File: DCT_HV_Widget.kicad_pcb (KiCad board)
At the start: 2 copper layers, 53.9 x 74.6 mm, 27 parts, among them J1 Control Voltage, J2 Bench Power Supply, J3 High Voltage, Q1 ZXTN10150D, U1 LT1468CS8-PBF, U2 OC150G

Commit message: Updated PCB. Rearranged bottom silkscreen layer.
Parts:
- moved G*** 9.75 mm to (160.9, 100.1)
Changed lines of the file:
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@@
       (drillshape 0)
       (scaleselection 1)
-      (outputdirectory "FLoBBr_Gerbers")
+      (outputdirectory "FLoBBr_Drill")
     )
   )
@@
   )
   (footprint "LOGO" (layer "B.Cu")
-    (at 163.615556 109.435583 180)
+    (at 160.875 100.075 180)
     (attr board_only exclude_from_pos_files exclude_from_bom)
     (fp_text reference "G***" (at 0 0) (layer "B.SilkS") hide
@@
   (gr_line (start 166.116 72.644) (end 175.768 72.644) (layer "F.SilkS") (width 0.15))
   (gr_rect (start 133.425 69.4) (end 187.375 144) (layer "Edge.Cuts") (width 0.1016) (fill none))
-  (gr_text "Fantastic Load Bearing Board\n(FLoBBr)" (at 159.766 83.058) (layer "B.SilkS")
-    (effects (font (size 2 2) (thickness 0.4)) (justify mirror))
+  (gr_text "Fantastic Load Bearing Board\n(FLoBBr)" (at 183.875 112.7 90) (layer "B.SilkS")
+    (effects (font (size 1.75 1.75) (thickness 0.3)) (justify mirror))
   )
   (gr_text "+" (at 146.925 89.15) (layer "F.SilkS")

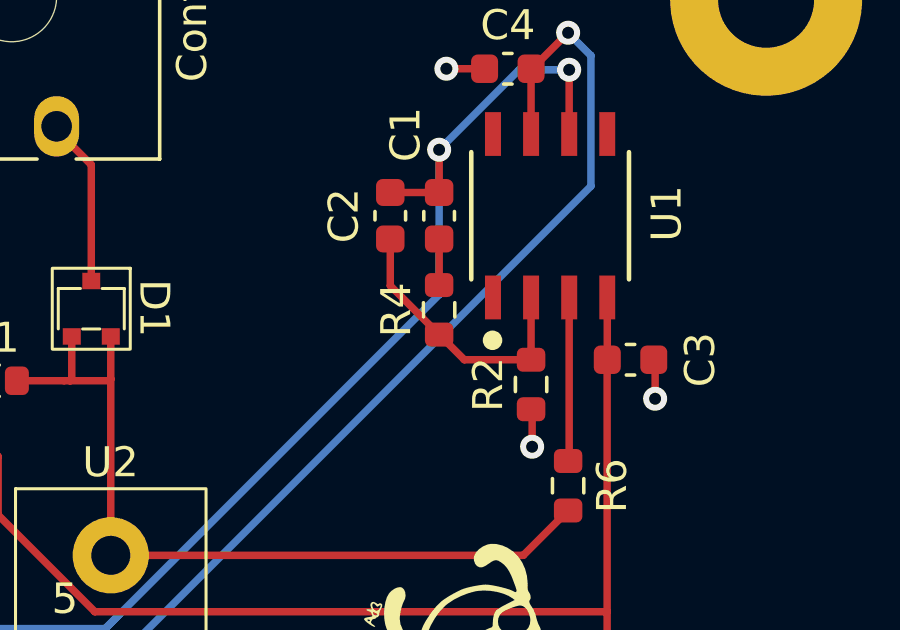
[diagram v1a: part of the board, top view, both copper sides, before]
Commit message: Updated PCB. Rotated R4. Minimize distance between R4 and C2.
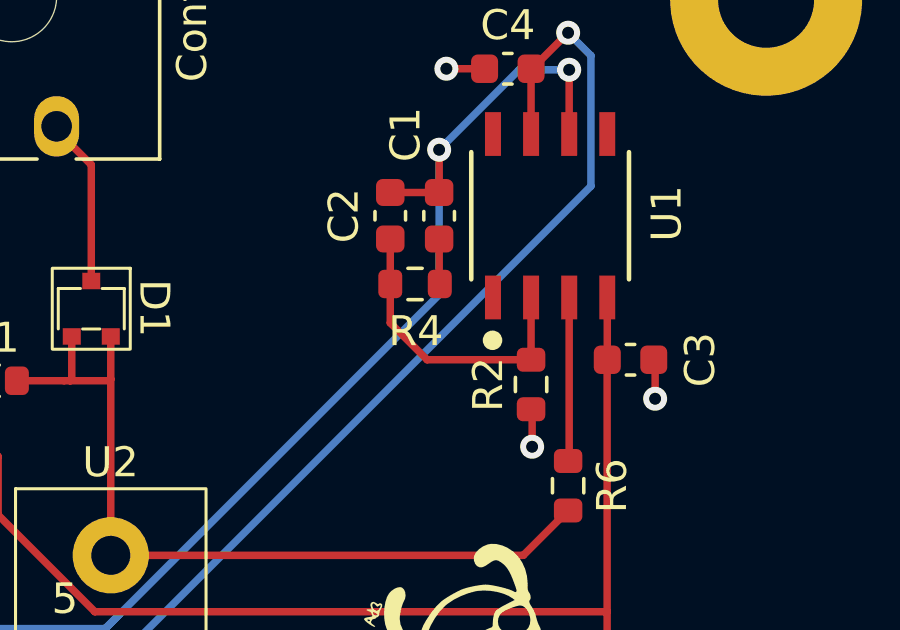
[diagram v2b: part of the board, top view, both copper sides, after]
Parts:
- moved R4 1.18 mm to (170.5, 84.0), turned to 0 degrees
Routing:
- net Net-(C2-Pad1): track 9.35 -> 9.91 mm
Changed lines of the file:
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@@
   )
   (footprint "Resistor_SMD:R_0603_1608Metric" (layer "F.Cu")
-    (at 171.3 84.836 90)
+    (at 170.497 83.975)
     (descr "Resistor SMD 0603 (1608 Metric), square (rectangular) end terminal, IPC_7351 nominal, (Body size source: IPC-SM-782 page 72, https://www.pcb-3d.com/wordpress/wp-content/uploads/ipc-sm-782a_amendment_1_and_2.pdf), generated with kicad-footprint-generator")
     (tags "resistor")
@@
     (property "Sheetname" "")
     (attr smd)
-    (fp_text reference "R4" (at 0 -1.43 90) (layer "F.SilkS")
+    (fp_text reference "R4" (at 0.028 1.575) (layer "F.SilkS")
       (effects (font (size 1 1) (thickness 0.15)))
     )
-    (fp_text value "1.54k" (at 0 1.43 90) (layer "F.Fab")
+    (fp_text value "1.54k" (at 0 1.43) (layer "F.Fab")
       (effects (font (size 1 1) (thickness 0.15)))
     )
-    (fp_text user "${REFERENCE}" (at 0 0 90) (layer "F.Fab")
+    (fp_text user "${REFERENCE}" (at 0 0) (layer "F.Fab")
       (effects (font (size 0.4 0.4) (thickness 0.06)))
     )
@@
     (fp_line (start 0.8 -0.4125) (end 0.8 0.4125) (layer "F.Fab") (width 0.1))
     (fp_line (start -0.8 -0.4125) (end 0.8 -0.4125) (layer "F.Fab") (width 0.1))
-    (pad "1" smd roundrect (at -0.825 0 90) (size 0.8 0.95) (layers "F.Cu" "F.Paste" "F.Mask") (roundrect_rratio 0.25)
+    (pad "1" smd roundrect (at -0.825 0) (size 0.8 0.95) (layers "F.Cu" "F.Paste" "F.Mask") (roundrect_rratio 0.25)
       (net 3 "Net-(C2-Pad1)") (pintype "passive"))
-    (pad "2" smd roundrect (at 0.825 0 90) (size 0.8 0.95) (layers "F.Cu" "F.Paste" "F.Mask") (roundrect_rratio 0.25)
+    (pad "2" smd roundrect (at 0.825 0) (size 0.8 0.95) (layers "F.Cu" "F.Paste" "F.Mask") (roundrect_rratio 0.25)
       (net 1 "Net-(C1-Pad1)") (pintype "passive"))
     (model "${KICAD6_3DMODEL_DIR}/Resistor_SMD.3dshapes/R_0603_1608Metric.wrl"
@@
   (segment (start 171.3 84.330671) (end 171.3 79.5) (width 0.25) (layer "B.Cu") (net 2))
   (segment (start 160.205671 95.425) (end 160.652835 94.977835) (width 0.25) (layer "B.Cu") (net 2))
+  (segment (start 169.672 84.2) (end 169.672 85.272) (width 0.25) (layer "F.Cu") (net 3))
   (segment (start 174.365 86.5) (end 174.365 84.42415) (width 0.25) (layer "F.Cu") (net 3))
+  (segment (start 169.672 85.272) (end 170.9 86.5) (width 0.25) (layer "F.Cu") (net 3))
   (segment (start 169.672 82.475) (end 169.672 84.033) (width 0.25) (layer "F.Cu") (net 3))
-  (segment (start 169.672 84.033) (end 171.3 85.661) (width 0.25) (layer "F.Cu") (net 3))
-  (segment (start 172.139 86.5) (end 174.365 86.5) (width 0.25) (layer "F.Cu") (net 3))
-  (segment (start 171.3 85.661) (end 172.139 86.5) (width 0.25) (layer "F.Cu") (net 3))
+  (segment (start 170.9 86.5) (end 174.365 86.5) (width 0.25) (layer "F.Cu") (net 3))
   (segment (start 174.4 89.4) (end 174.4 88.185) (width 0.25) (layer "F.Cu") (net 4))
   (segment (start 178.5 86.545) (end 178.455 86.5) (width 0.25) (layer "F.Cu") (net 4))

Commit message: Ready for fab. FLoBBr rev1
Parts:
- moved C2 7.58 mm to (172.9, 88.6), turned to -90 degrees
- moved C1 6.88 mm to (171.2, 88.6), turned to -90 degrees
- moved R4 2.78 mm to (172.1, 86.3), turned to 180 degrees
- moved R2 0.30 mm to (174.4, 87.0)
- moved C3 0.23 mm to (177.7, 86.3)
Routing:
- net Net-(C2-Pad1): track 9.91 -> 4.82 mm
- net Net-(C1-Pad2): track 43.0 -> 45.2 mm
- net /VP6: track 52.2 -> 51.6 mm
